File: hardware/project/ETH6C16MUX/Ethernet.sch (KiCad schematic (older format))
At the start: 38 parts, among them U201 LC03-3.3, U202 LAN8742, U203 LC03-3.3, U204 SR3.3, U205 SR3.3, U206 ASDM1-50.000MHZ-LC-T

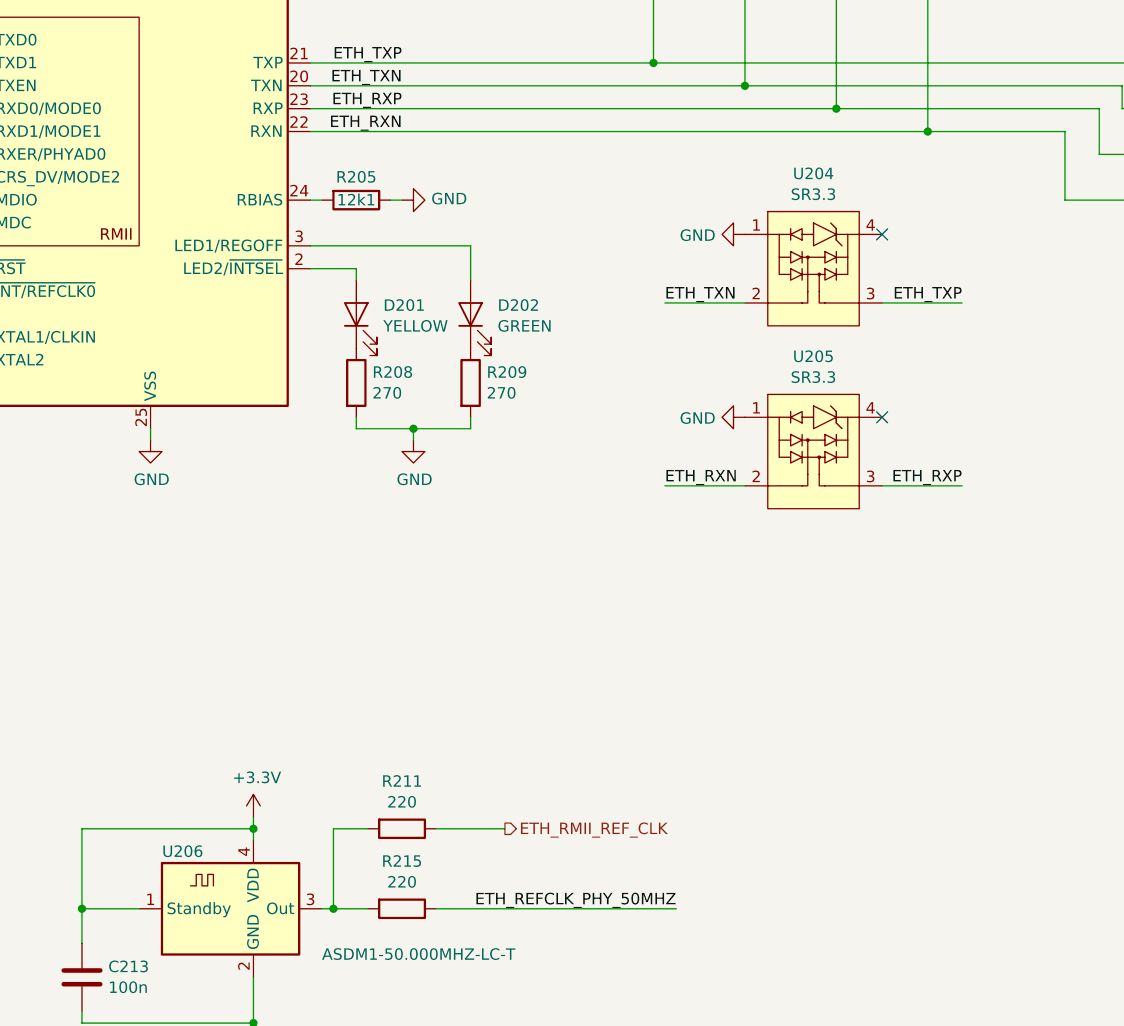
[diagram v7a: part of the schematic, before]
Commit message: Deleted FPGA part and change it for SPI IO chips. Change power supply circuit.
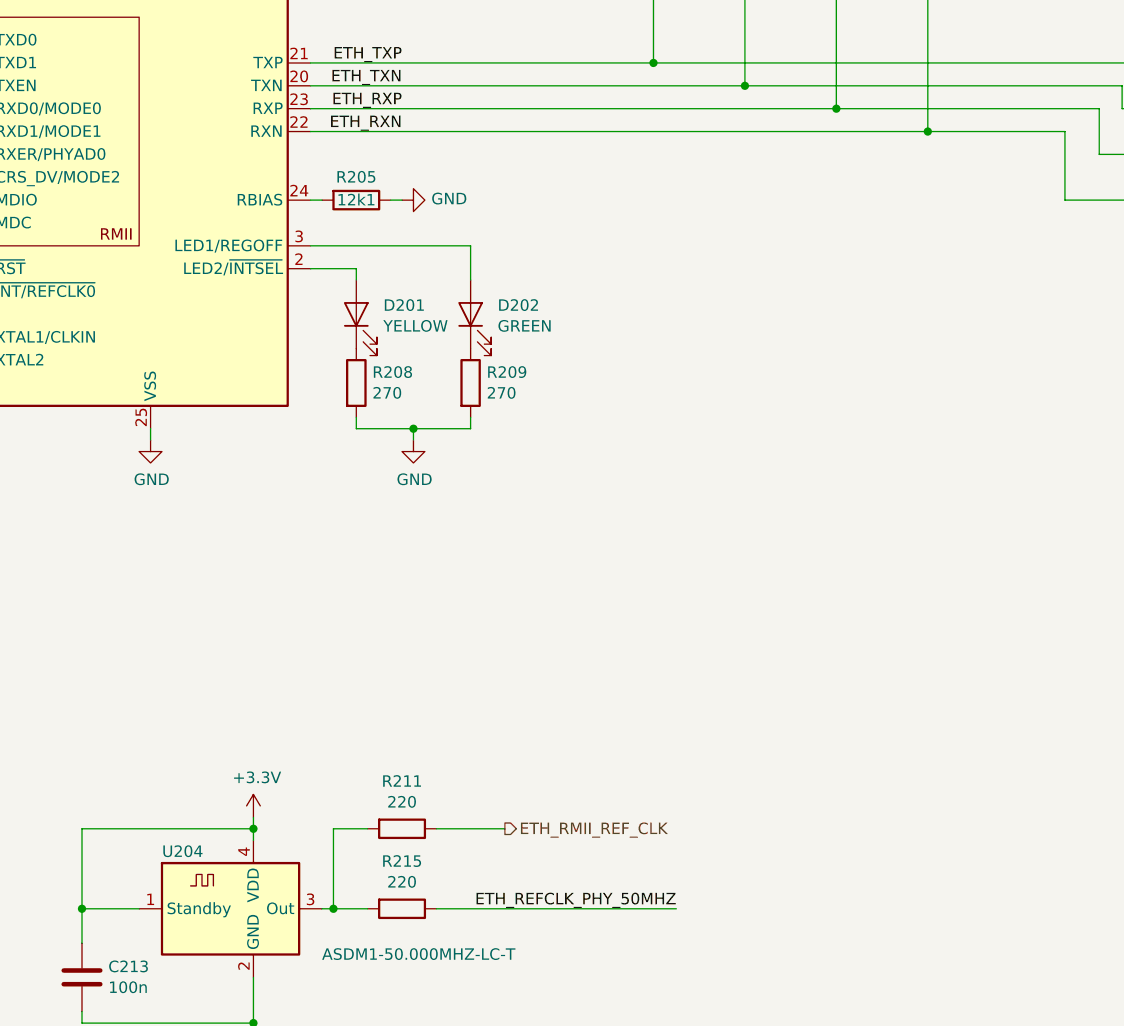
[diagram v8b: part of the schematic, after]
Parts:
- removed U204, U205: SR3.3, Package_TO_SOT_SMD:SOT-143, symbol ETH6C16MUX:SR3.3
- C201, C202, C204, C205, C206, C207, C210, C213: footprint ETH6C16MXU:C_0603_A_Pad1.05x0.95mm_HandSolder -> Capacitor_SMD:C_0603_1608Metric_Pad1.05x0.95mm_HandSolder
- C203, C209: footprint ETH6C16MXU:C_0603_B_Pad1.05x0.95mm_HandSolder -> Capacitor_SMD:C_0603_1608Metric_Pad1.05x0.95mm_HandSolder
- FB201: footprint ETH6C16MXU:R_0805_D_Pad1.15x1.40mm_HandSolder -> Resistor_SMD:R_0805_2012Metric_Pad1.15x1.40mm_HandSolder
- R208, R209, R212, R213, R214: footprint ETH6C16MXU:R_0603_E_Pad1.05x0.95mm_HandSolder -> Resistor_SMD:R_0603_1608Metric_Pad1.05x0.95mm_HandSolder
- renumbered U206 to U204
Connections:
- no-connect marks 11 -> 9
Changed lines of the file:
@@
 $Descr A4 11693 8268
 encoding utf-8
-Sheet 2 7
+Sheet 2 6
 Title "Ethernet"
 Date ""
@@
 F 0 "R208" H 4070 4346 50  0000 L CNN
 F 1 "270" H 4070 4255 50  0000 L CNN
-F 2 "ETH6C16MXU:R_0603_E_Pad1.05x0.95mm_HandSolder" V 3930 4300 50  0001 C CNN
+F 2 "Resistor_SMD:R_0603_1608Metric_Pad1.05x0.95mm_HandSolder" V 3930 4300 50  0001 C CNN
 F 3 "~" H 4000 4300 50  0001 C CNN
 	1    4000 4300
@@
 F 0 "R209" H 4570 4346 50  0000 L CNN
 F 1 "270" H 4570 4255 50  0000 L CNN
-F 2 "ETH6C16MXU:R_0603_E_Pad1.05x0.95mm_HandSolder" V 4430 4300 50  0001 C CNN
+F 2 "Resistor_SMD:R_0603_1608Metric_Pad1.05x0.95mm_HandSolder" V 4430 4300 50  0001 C CNN
 F 3 "~" H 4500 4300 50  0001 C CNN
 	1    4500 4300
@@
 F 0 "C209" H 2365 1996 50  0000 L CNN
 F 1 "1u" H 2365 1905 50  0000 L CNN
-F 2 "ETH6C16MXU:C_0603_B_Pad1.05x0.95mm_HandSolder" H 2288 1800 50  0001 C CNN
+F 2 "Capacitor_SMD:C_0603_1608Metric_Pad1.05x0.95mm_HandSolder" H 2288 1800 50  0001 C CNN
 F 3 "~" H 2250 1950 50  0001 C CNN
 	1    2250 1950
@@
 	8700 4050 8950 4050
 $Comp
-L power:Earth #PWR0214
+L power:Earth #PWR0212
 U 1 1 5D79DEAE
 P 8700 4450
-F 0 "#PWR0214" H 8700 4200 50  0001 C CNN
+F 0 "#PWR0212" H 8700 4200 50  0001 C CNN
 F 1 "Earth" H 8700 4300 50  0001 C CNN
 F 2 "" H 8700 4450 50  0001 C CNN
@@
 F 0 "C210" H 7565 3896 50  0000 L CNN
 F 1 "100n" H 7565 3805 50  0000 L CNN
-F 2 "ETH6C16MXU:C_0603_A_Pad1.05x0.95mm_HandSolder" H 7488 3700 50  0001 C CNN
+F 2 "Capacitor_SMD:C_0603_1608Metric_Pad1.05x0.95mm_HandSolder" H 7488 3700 50  0001 C CNN
 F 3 "~" H 7450 3850 50  0001 C CNN
 	1    7450 3850
@@
 	8200 4900 8100 4900
 $Comp
-L power:Earth #PWR0218
+L power:Earth #PWR0216
 U 1 1 5D7A6317
 P 8200 5100
-F 0 "#PWR0218" H 8200 4850 50  0001 C CNN
+F 0 "#PWR0216" H 8200 4850 50  0001 C CNN
 F 1 "Earth" H 8200 4950 50  0001 C CNN
 F 2 "" H 8200 5100 50  0001 C CNN
@@
 F 0 "C201" H 1915 1296 50  0000 L CNN
 F 1 "100n" H 1915 1205 50  0000 L CNN
-F 2 "ETH6C16MXU:C_0603_A_Pad1.05x0.95mm_HandSolder" H 1838 1100 50  0001 C CNN
+F 2 "Capacitor_SMD:C_0603_1608Metric_Pad1.05x0.95mm_HandSolder" H 1838 1100 50  0001 C CNN
 F 3 "~" H 1800 1250 50  0001 C CNN
 	1    1800 1250
@@
 F 0 "C202" H 2365 1296 50  0000 L CNN
 F 1 "100n" H 2365 1205 50  0000 L CNN
-F 2 "ETH6C16MXU:C_0603_A_Pad1.05x0.95mm_HandSolder" H 2288 1100 50  0001 C CNN
+F 2 "Capacitor_SMD:C_0603_1608Metric_Pad1.05x0.95mm_HandSolder" H 2288 1100 50  0001 C CNN
 F 3 "~" H 2250 1250 50  0001 C CNN
 	1    2250 1250
@@
 F 0 "FB201" V 2826 1050 50  0000 C CNN
 F 1 "742792031" V 2917 1050 50  0000 C CNN
-F 2 "ETH6C16MXU:R_0805_D_Pad1.15x1.40mm_HandSolder" V 3030 1050 50  0001 C CNN
+F 2 "Resistor_SMD:R_0805_2012Metric_Pad1.15x1.40mm_HandSolder" V 3030 1050 50  0001 C CNN
 F 3 "~" H 3100 1050 50  0001 C CNN
 	1    3100 1050
@@
 F 0 "C203" H 3465 1296 50  0000 L CNN
 F 1 "1u" H 3465 1205 50  0000 L CNN
-F 2 "ETH6C16MXU:C_0603_B_Pad1.05x0.95mm_HandSolder" H 3388 1100 50  0001 C CNN
+F 2 "Capacitor_SMD:C_0603_1608Metric_Pad1.05x0.95mm_HandSolder" H 3388 1100 50  0001 C CNN
 F 3 "~" H 3350 1250 50  0001 C CNN
 	1    3350 1250
@@
 F 0 "C204" H 3915 1296 50  0000 L CNN
 F 1 "100n" H 3915 1205 50  0000 L CNN
-F 2 "ETH6C16MXU:C_0603_A_Pad1.05x0.95mm_HandSolder" H 3838 1100 50  0001 C CNN
+F 2 "Capacitor_SMD:C_0603_1608Metric_Pad1.05x0.95mm_HandSolder" H 3838 1100 50  0001 C CNN
 F 3 "~" H 3800 1250 50  0001 C CNN
 	1    3800 1250
@@
 F 0 "C205" H 4365 1296 50  0000 L CNN
 F 1 "100n" H 4365 1205 50  0000 L CNN
-F 2 "ETH6C16MXU:C_0603_A_Pad1.05x0.95mm_HandSolder" H 4288 1100 50  0001 C CNN
+F 2 "Capacitor_SMD:C_0603_1608Metric_Pad1.05x0.95mm_HandSolder" H 4288 1100 50  0001 C CNN
 F 3 "~" H 4250 1250 50  0001 C CNN
 	1    4250 1250
@@
 F 0 "C206" H 4965 1296 50  0000 L CNN
 F 1 "100n" H 4965 1205 50  0000 L CNN
-F 2 "ETH6C16MXU:C_0603_A_Pad1.05x0.95mm_HandSolder" H 4888 1100 50  0001 C CNN
+F 2 "Capacitor_SMD:C_0603_1608Metric_Pad1.05x0.95mm_HandSolder" H 4888 1100 50  0001 C CNN
 F 3 "~" H 4850 1250 50  0001 C CNN
 	1    4850 1250
@@
 F 0 "C207" H 7115 1296 50  0000 L CNN
 F 1 "100n" H 7115 1205 50  0000 L CNN
-F 2 "ETH6C16MXU:C_0603_A_Pad1.05x0.95mm_HandSolder" H 7038 1100 50  0001 C CNN
+F 2 "Capacitor_SMD:C_0603_1608Metric_Pad1.05x0.95mm_HandSolder" H 7038 1100 50  0001 C CNN
 F 3 "~" H 7000 1250 50  0001 C CNN
 	1    7000 1250
@@
 F 0 "R212" H 1520 6496 50  0000 L CNN
 F 1 "10k" H 1520 6405 50  0000 L CNN
-F 2 "ETH6C16MXU:R_0603_E_Pad1.05x0.95mm_HandSolder" V 1380 6450 50  0001 C CNN
+F 2 "Resistor_SMD:R_0603_1608Metric_Pad1.05x0.95mm_HandSolder" V 1380 6450 50  0001 C CNN
 F 3 "~" H 1450 6450 50  0001 C CNN
 	1    1450 6450
@@
 F 0 "R213" H 1870 6496 50  0000 L CNN
 F 1 "10k" H 1870 6405 50  0000 L CNN
-F 2 "ETH6C16MXU:R_0603_E_Pad1.05x0.95mm_HandSolder" V 1730 6450 50  0001 C CNN
+F 2 "Resistor_SMD:R_0603_1608Metric_Pad1.05x0.95mm_HandSolder" V 1730 6450 50  0001 C CNN
 F 3 "~" H 1800 6450 50  0001 C CNN
 	1    1800 6450
@@
 F 0 "R214" H 2220 6496 50  0000 L CNN
 F 1 "10k" H 2220 6405 50  0000 L CNN
-F 2 "ETH6C16MXU:R_0603_E_Pad1.05x0.95mm_HandSolder" V 2080 6450 50  0001 C CNN
+F 2 "Resistor_SMD:R_0603_1608Metric_Pad1.05x0.95mm_HandSolder" V 2080 6450 50  0001 C CNN
 F 3 "~" H 2150 6450 50  0001 C CNN
 	1    2150 6450
@@
 Wire Wire Line
 	2300 4100 1250 4100
-$Comp
-L ETH6C16MUX:SR3.3 U205
-U 1 1 5D9B1A51
-P 6000 4600
-F 0 "U205" H 6000 5015 50  0000 C CNN
-F 1 "SR3.3" H 6000 4924 50  0000 C CNN
-F 2 "Package_TO_SOT_SMD:SOT-143" H 6125 4800 50  0001 C CNN
-F 3 "" H 6125 4800 50  0001 C CNN
-	1    6000 4600
-	1    0    0    -1
-$EndComp
-$Comp
-L ETH6C16MUX:SR3.3 U204
-U 1 1 5D9B4299
-P 6000 3800
-F 0 "U204" H 6000 4215 50  0000 C CNN
-F 1 "SR3.3" H 6000 4124 50  0000 C CNN
-F 2 "Package_TO_SOT_SMD:SOT-143" H 6125 4000 50  0001 C CNN
-F 3 "" H 6125 4000 50  0001 C CNN
-	1    6000 3800
-	1    0    0    -1
-$EndComp
-NoConn ~ 6300 3650
-NoConn ~ 6300 4450
-Text Label 6650 3950 2    50   ~ 0
-ETH_TXP
-Text Label 5350 3950 0    50   ~ 0
-ETH_TXN
-Text Label 6650 4750 2    50   ~ 0
-ETH_RXP
-Text Label 5350 4750 0    50   ~ 0
-ETH_RXN
-Wire Wire Line
-	5700 4750 5350 4750
-Wire Wire Line
-	6650 4750 6300 4750
-Wire Wire Line
-	5700 3950 5350 3950
-Wire Wire Line
-	6650 3950 6300 3950
 Wire Notes Line
 	7950 6450 7950 5100
@@
 F 0 "C213" H 2915 6946 50  0000 L CNN
 F 1 "100n" H 2915 6855 50  0000 L CNN
-F 2 "ETH6C16MXU:C_0603_A_Pad1.05x0.95mm_HandSolder" H 2838 6750 50  0001 C CNN
+F 2 "Capacitor_SMD:C_0603_1608Metric_Pad1.05x0.95mm_HandSolder" H 2838 6750 50  0001 C CNN
 F 3 "~" H 2800 6900 50  0001 C CNN
 	1    2800 6900
@@
 ETH_RMII_REF_CLK
 $Comp
-L Oscillator:ASDMB-xxxMHz U206
+L Oscillator:ASDMB-xxxMHz U204
 U 1 1 5DB0D8D2
 P 3450 6600
-F 0 "U206" H 3150 6850 50  0000 L CNN
+F 0 "U204" H 3150 6850 50  0000 L CNN
 F 1 "ASDM1-50.000MHZ-LC-T" H 3850 6400 50  0000 L CNN
 F 2 "Oscillator:Oscillator_SMD_Abracon_ASDMB-4Pin_2.5x2.0mm" H 3450 6600 50  0001 C CNN
@@
 	3550 7100 3550 6900
 $Comp
-L power:GND #PWR0215
+L power:GND #PWR0213
 U 1 1 5DBA4079
 P 3100 4550
-F 0 "#PWR0215" H 3100 4300 50  0001 C CNN
+F 0 "#PWR0213" H 3100 4300 50  0001 C CNN
 F 1 "GND" H 3105 4377 50  0000 C CNN
 F 2 "" H 3100 4550 50  0001 C CNN
@@
 $EndComp
 $Comp
-L power:GND #PWR0216
+L power:GND #PWR0214
 U 1 1 5DBA4651
 P 4250 4550
-F 0 "#PWR0216" H 4250 4300 50  0001 C CNN
+F 0 "#PWR0214" H 4250 4300 50  0001 C CNN
 F 1 "GND" H 4255 4377 50  0000 C CNN
 F 2 "" H 4250 4550 50  0001 C CNN
@@
 $EndComp
 $Comp
-L power:GND #PWR0211
-U 1 1 5DBA709B
-P 5700 3650
-F 0 "#PWR0211" H 5700 3400 50  0001 C CNN
-F 1 "GND" V 5705 3522 50  0000 R CNN
-F 2 "" H 5700 3650 50  0001 C CNN
-F 3 "" H 5700 3650 50  0001 C CNN
-	1    5700 3650
-	0    1    1    0
-$EndComp
-$Comp
-L power:GND #PWR0213
-U 1 1 5DBA763A
-P 5700 4450
-F 0 "#PWR0213" H 5700 4200 50  0001 C CNN
-F 1 "GND" V 5705 4322 50  0000 R CNN
-F 2 "" H 5700 4450 50  0001 C CNN
-F 3 "" H 5700 4450 50  0001 C CNN
-	1    5700 4450
-	0    1    1    0
-$EndComp
-$Comp
 L power:GND #PWR0209
 U 1 1 5DBAA3D5
@@
 $EndComp
 $Comp
-L power:GND #PWR0212
+L power:GND #PWR0211
 U 1 1 5DBAD404
 P 7450 4050
-F 0 "#PWR0212" H 7450 3800 50  0001 C CNN
+F 0 "#PWR0211" H 7450 3800 50  0001 C CNN
 F 1 "GND" H 7455 3877 50  0000 C CNN
 F 2 "" H 7450 4050 50  0001 C CNN
@@
 $EndComp
 $Comp
-L power:GND #PWR0217
+L power:GND #PWR0215
 U 1 1 5DBAF536
 P 7700 5100
-F 0 "#PWR0217" H 7700 4850 50  0001 C CNN
+F 0 "#PWR0215" H 7700 4850 50  0001 C CNN
 F 1 "GND" H 7705 4927 50  0000 C CNN
 F 2 "" H 7700 5100 50  0001 C CNN
@@
 $EndComp
 $Comp
-L power:GND #PWR0221
+L power:GND #PWR0219
 U 1 1 5DBB2260
 P 3550 7150
-F 0 "#PWR0221" H 3550 6900 50  0001 C CNN
+F 0 "#PWR0219" H 3550 6900 50  0001 C CNN
 F 1 "GND" H 3555 6977 50  0000 C CNN
 F 2 "" H 3550 7150 50  0001 C CNN
@@
 $EndComp
 $Comp
-L power:+3.3V #PWR0219
+L power:+3.3V #PWR0217
 U 1 1 5DACAFF6
 P 1800 6200
-F 0 "#PWR0219" H 1800 6050 50  0001 C CNN
+F 0 "#PWR0217" H 1800 6050 50  0001 C CNN
 F 1 "+3.3V" H 1815 6373 50  0000 C CNN
 F 2 "" H 1800 6200 50  0001 C CNN
@@
 $EndComp
 $Comp
-L power:+3.3V #PWR0220
+L power:+3.3V #PWR0218
 U 1 1 5DACB3A2
 P 3550 6200
-F 0 "#PWR0220" H 3550 6050 50  0001 C CNN
+F 0 "#PWR0218" H 3550 6050 50  0001 C CNN
 F 1 "+3.3V" H 3565 6373 50  0000 C CNN
 F 2 "" H 3550 6200 50  0001 C CNN
